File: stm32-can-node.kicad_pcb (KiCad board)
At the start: 4 copper layers, 40 x 25 mm, 47 parts, among them J1 Conn_01x04_Pin, J2 Conn_01x11_Pin, J3 Conn_01x11_Pin, J4 Conn_01x05_Pin, U1 DS2484R+T, U3_1 STM32U535CEUxQ, U4 SN65HVD234DR, U5 AP63203WU-7, Y1 16MHz

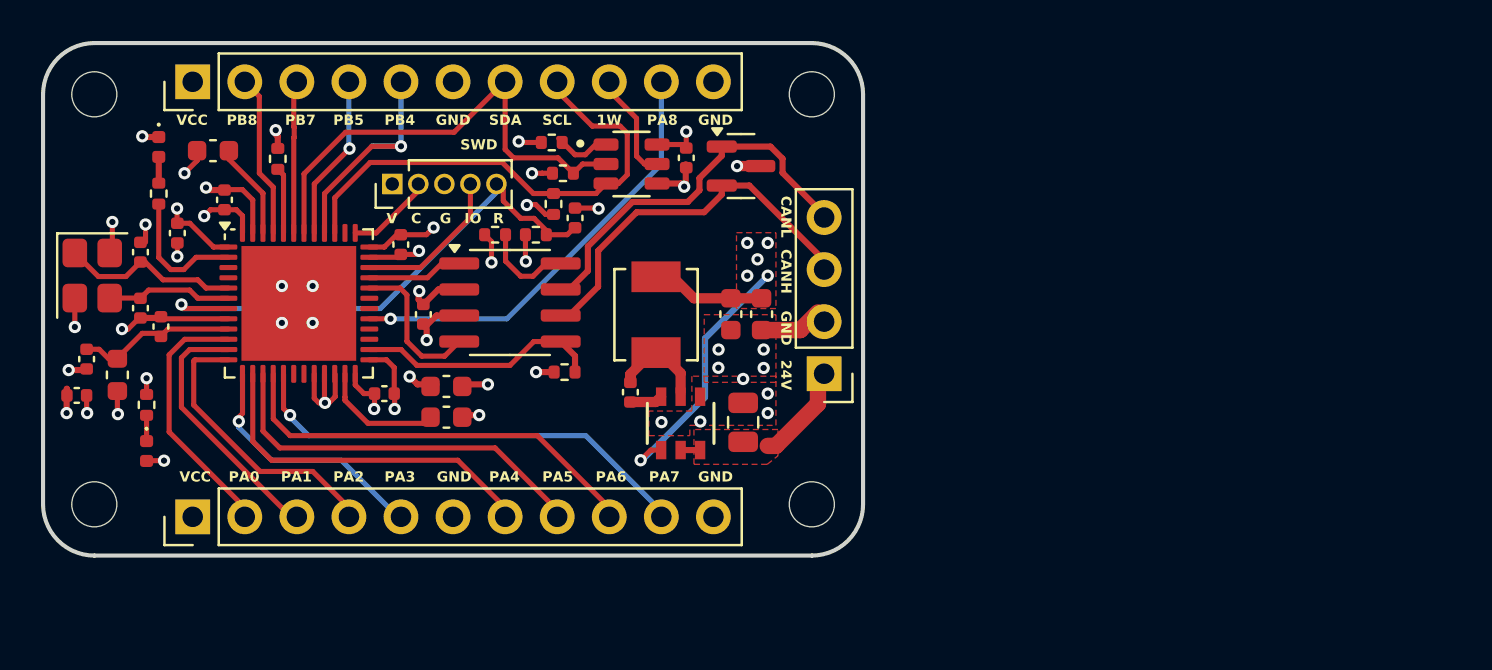
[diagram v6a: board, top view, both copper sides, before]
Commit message: added uart header
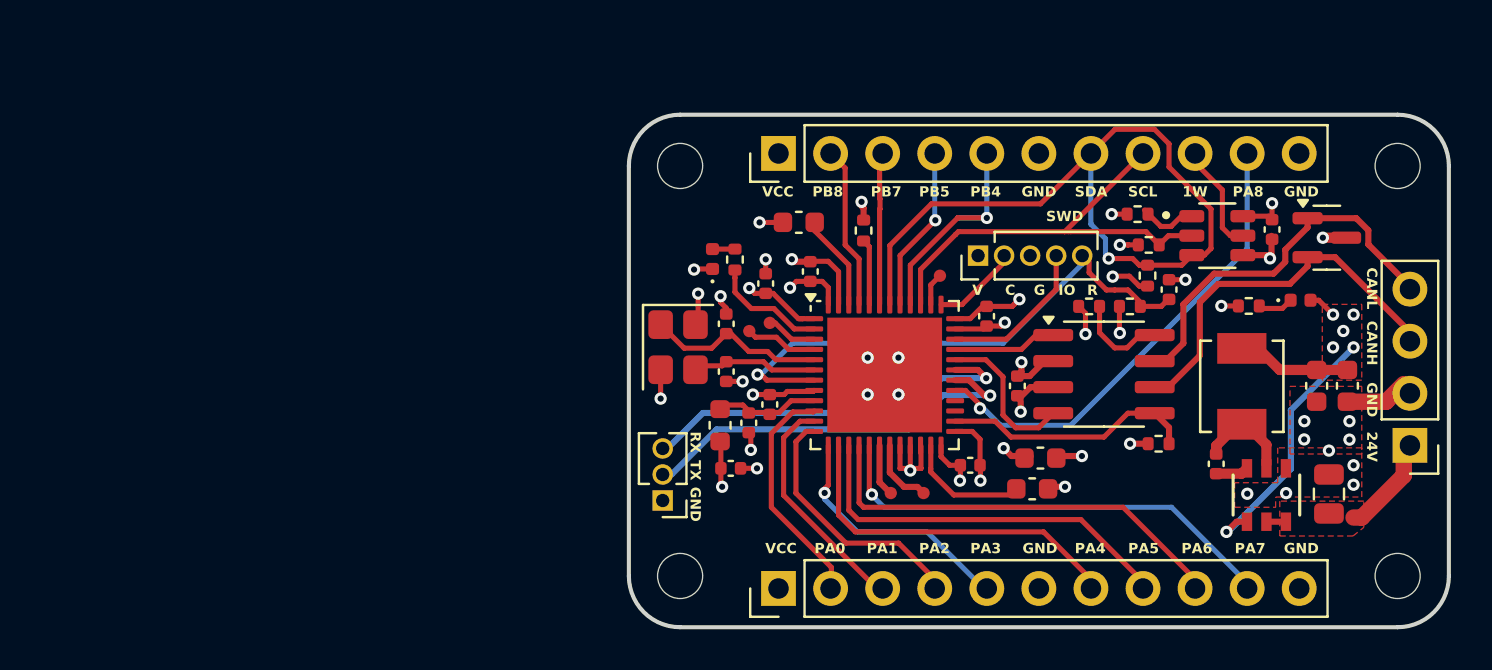
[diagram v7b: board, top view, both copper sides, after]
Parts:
- added J5: Conn_01x03_Pin, Connector_PinHeader_1.27mm:PinHeader_1x03_P1.27mm_Vertical, F.Cu at (90.1, 69.5)
- added TP1: TestPoint, mrk:mini_test_point, F.Cu at (103.6, 53.7)
- added TP2: TestPoint, mrk:mini_test_point, F.Cu at (102.8, 73.9)
- added TP3: TestPoint, mrk:mini_test_point, F.Cu at (101.2, 73.9)
- added TP4: TestPoint, mrk:mini_test_point, F.Cu at (95.3, 56.0)
- added TP5: TestPoint, mrk:mini_test_point, F.Cu at (94.3, 56.4)
- moved D1 56.8 mm to (121.2, 59.7), turned to 0 degrees
- moved R1 54.0 mm to (118.7, 60.0), turned to 180 degrees
- moved C9 32.4 mm to (94.3, 65.7)
- moved C10 32.1 mm to (93.4, 67.9), turned to 0 degrees
- moved C8 29.9 mm to (95.3, 64.8)
- moved FB1 29.5 mm to (92.9, 65.8)
- moved C11 29.2 mm to (114.8, 59.2)
- moved C14 29.2 mm to (107.4, 63.9)
- moved C3 29.2 mm to (108.5, 67.4)
- moved R3 29.2 mm to (110.9, 60.0)
- moved R4 29.2 mm to (113.7, 58.5)
- moved R7 29.2 mm to (114.3, 66.7)
- moved R8 29.2 mm to (112.9, 60.0)
- moved U4 29.2 mm to (111.6, 63.3)
- moved C4 28.8 mm to (95.1, 58.9), turned to 90 degrees
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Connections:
- net Net-(C15-Pad1) renamed /VDD11_2
- net Net-(C30-Pad1) renamed /VDD11
- J3 pad 7: I2C_SDA -> I2C_SCL
- J3 pad 8: I2C_SCL -> I2C_SDA
- U3_1 pad 18: unconnected-(U3_1-PB0-Pad18) -> PB0
- U3_1 pad 19: unconnected-(U3_1-PB1-Pad19) -> PB1
- U3_1 pad 3: unconnected-(U3_1-PC14-Pad3) -> PC14
- U3_1 pad 30: unconnected-(U3_1-PA9-Pad30) -> UART_TX
- U3_1 pad 31: unconnected-(U3_1-PA10-Pad31) -> UART_RX
- U3_1 pad 38: unconnected-(U3_1-PA15-Pad38) -> PA15
- U3_1 pad 39: I2C_SCL -> I2C_SDA
- U3_1 pad 4: unconnected-(U3_1-PC15-Pad4) -> PC15
- U3_1 pad 42: I2C_SDA -> I2C_SCL
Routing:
- net UART_TX: track 0.00 -> 19.6 mm, vias 0 -> 1
- net UART_RX: track 0.00 -> 19.0 mm, vias 0 -> 1
- net I2C_SCL: track 24.0 -> 36.0 mm, vias 0 -> 1
- net PC15: track 0.00 -> 3.54 mm
- net PB1: track 0.00 -> 3.46 mm
- net GND: track 44.1 -> 41.4 mm, vias 36 -> 37
- net +3.3VA: track 7.70 -> 5.08 mm
- net PB0: track 0.00 -> 2.53 mm
- net PC14: track 0.00 -> 2.49 mm
- net PA8: track 20.9 -> 23.1 mm
- net PA15: track 0.00 -> 1.59 mm
- net PA2: track 13.5 -> 12.1 mm
- net PA1: track 12.4 -> 11.1 mm
- net PA0: track 12.2 -> 10.9 mm
- net NRST: track 25.4 -> 26.6 mm
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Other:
- board text added: "RX"
- board text added: "TX"

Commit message: final changes before production
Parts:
- H1, H2, H3, H4: value MountingHole -> MountingHole_Pad; footprint MountingHole:MountingHole_2.2mm_M2 -> MountingHole:MountingHole_2.2mm_M2_DIN965_Pad
- R4, R5: value 1.5kΩ -> 3.3kΩ
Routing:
- net PB4: track 12.1 -> 9.29 mm
- net +3.3V: track 46.8 -> 47.5 mm
- net NRST: track 26.6 -> 27.3 mm
- net GND: track 41.4 -> 41.1 mm, vias 37 -> 39
